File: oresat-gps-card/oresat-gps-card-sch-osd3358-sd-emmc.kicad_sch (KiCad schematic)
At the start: 65 parts, among them J4 DM3BT-DSF-PEJS, U1 OSD3358-512M-BSM, U8 TCAN330, U9 EMMC+RESET+5.1-COMPATIBLE-BA

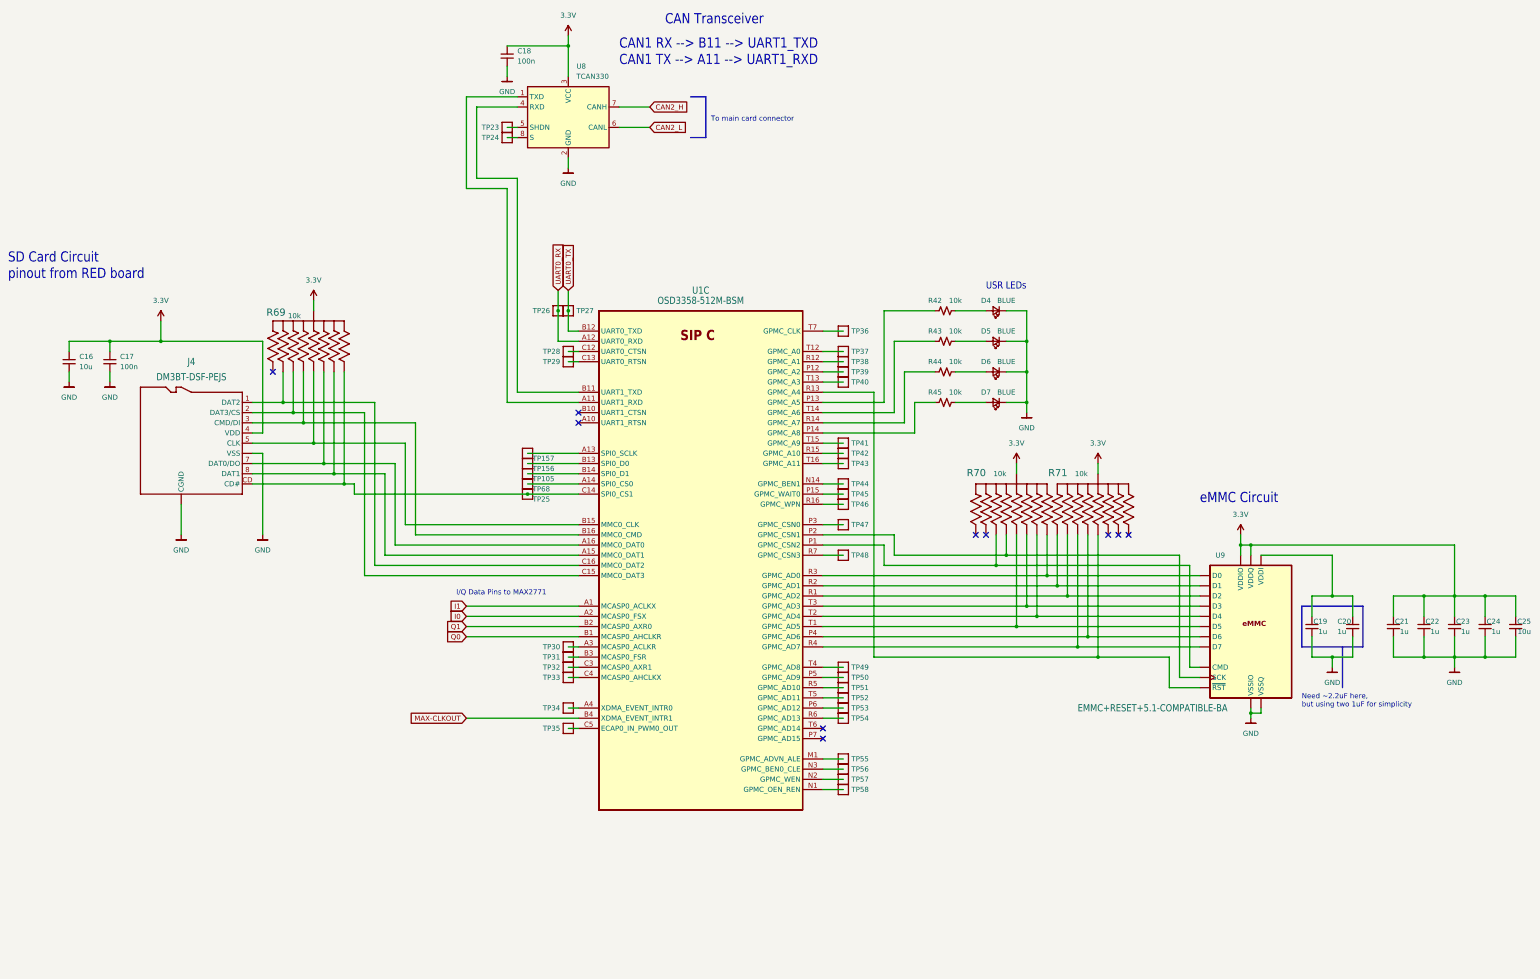
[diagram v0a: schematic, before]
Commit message: Cleaned up ERC and DRC errors on GPS card
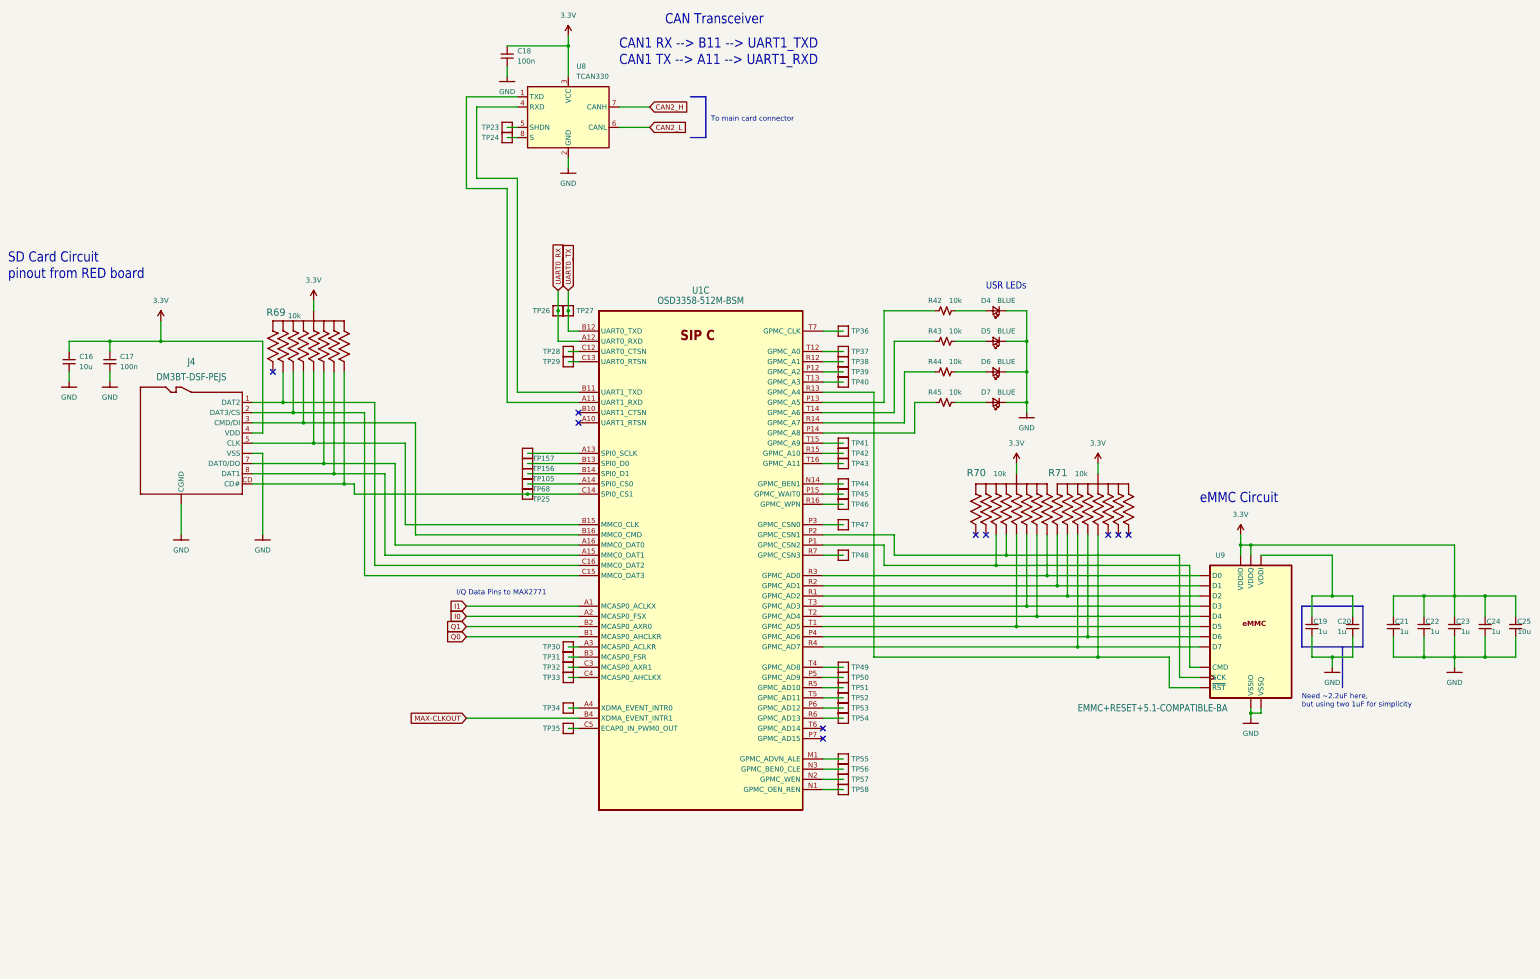
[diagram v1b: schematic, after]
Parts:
- J4: footprint oresat-footprints:J-Hirose-DM3BT-DSF-PEJS -> oresat-connectors:J-Hirose-DM3BT-DSF-PEJS
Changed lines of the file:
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@@
       (effects (font (size 1.778 1.5113)))
     )
-    (property "Footprint" "oresat-footprints:J-Hirose-DM3BT-DSF-PEJS" (at 66.04 129.54 0)
+    (property "Footprint" "oresat-connectors:J-Hirose-DM3BT-DSF-PEJS" (at 66.04 129.54 0)
       (effects (font (size 1.27 1.27)) hide)
     )

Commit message: Updated KiCAD 8, updated schematic sheet info, polished some schematic things, and made DNP parts DNP.
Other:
- title: (none) -> OreSat GPS Card

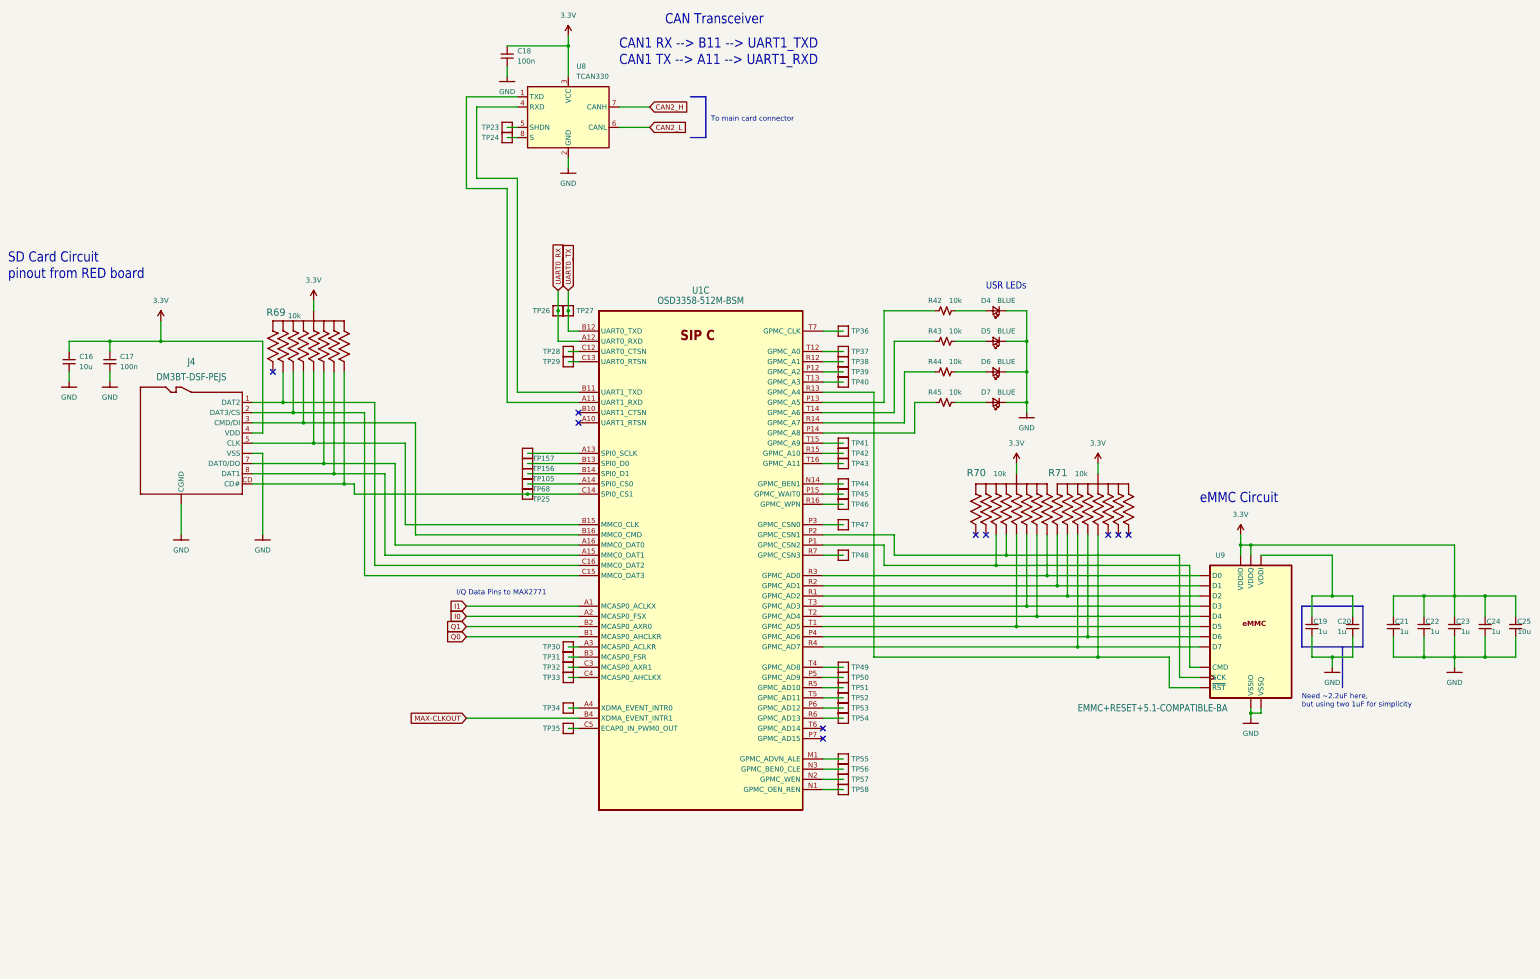
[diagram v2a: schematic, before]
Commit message: updated symbols and started new 2771 symbol
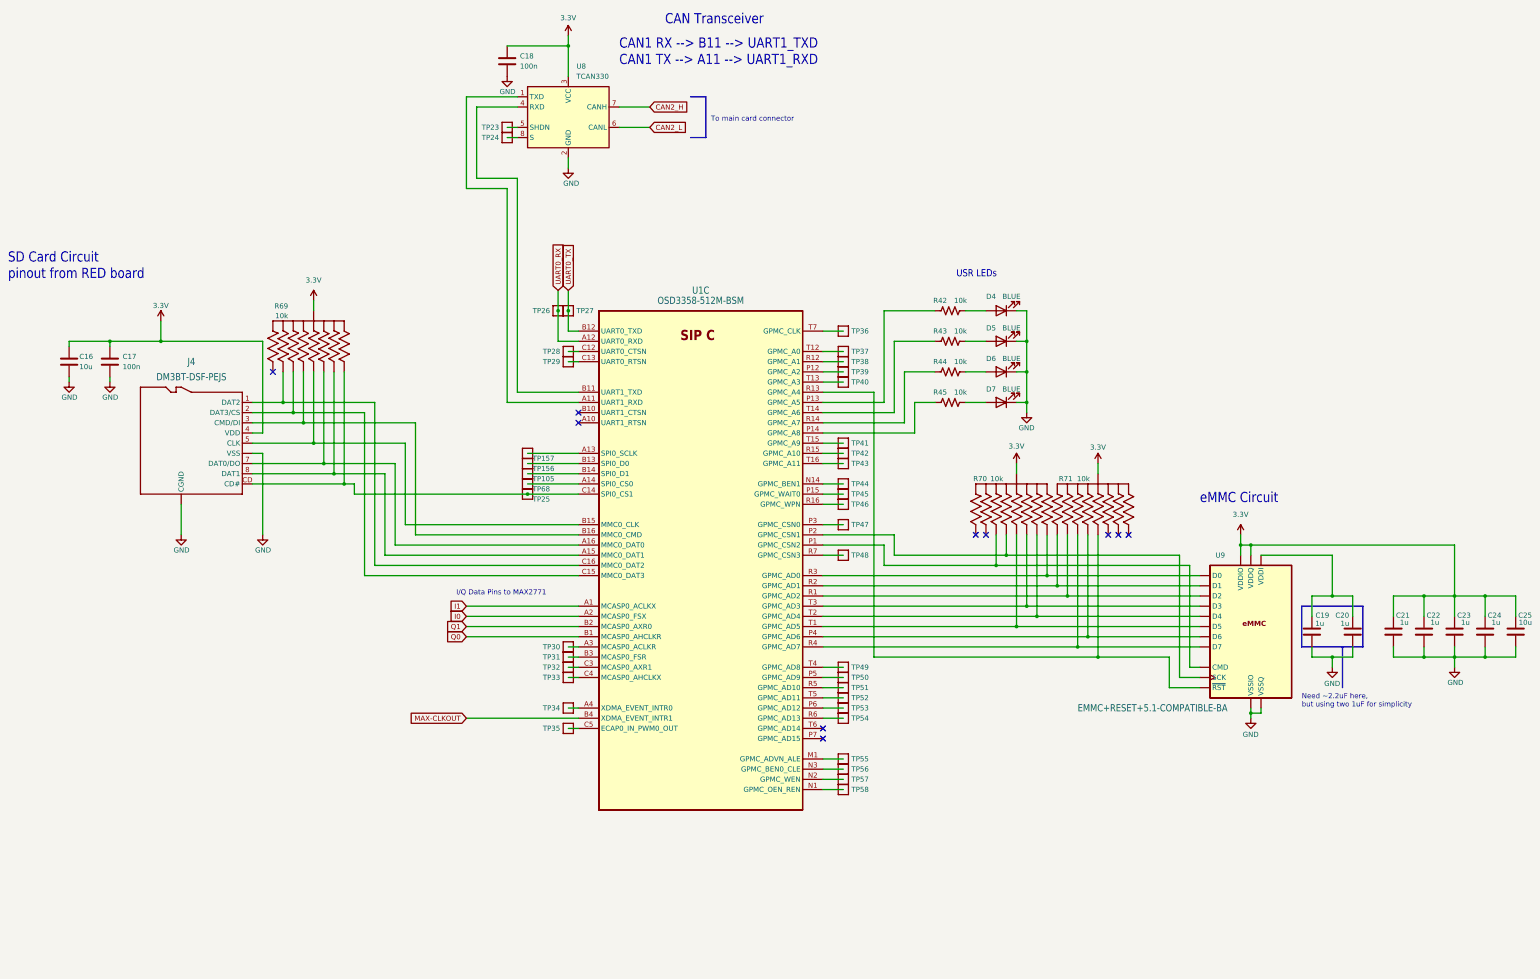
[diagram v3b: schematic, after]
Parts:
- C16, C17, C18, C19, C20, C21, C22, C23, C24, C25: symbol Device:C_Small -> Device:C
- D4, D5, D6, D7: symbol Device:LED_Small -> Device:LED
- R42, R43, R44, R45: symbol Device:R_Small_US -> Device:R_US
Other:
- moved on the sheet: C18, C19, C20, C21, C22, C23, C24, C25, D4, D5, D6, D7

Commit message: Routine Push
Various small changes made
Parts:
- removed TP105, TP156, TP157, TP23, TP24, TP25, TP28, TP29, TP30, TP31, TP32, TP33, TP34, TP35, TP36, TP37, TP38, TP39, TP40, TP41, TP42, TP43, TP44, TP45, TP46, TP47, TP48, TP49, TP50, TP51, TP52, TP53, TP54, TP55, TP56, TP57, TP58, TP68: 0.03x0.04, oresat-misc:TestPoint_Pad_D1.0mm, symbol oresat-misc:Test-Point-1mm-round
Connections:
- no-connect marks 10 -> 45

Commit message: Routine Push
First attempt to clean up schematic
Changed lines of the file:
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@@
 		)
 	)
-	(global_label "I1"
+	(hierarchical_label "Q0"
 		(shape input)
-		(at 134.62 170.18 180)
-		(fields_autoplaced yes)
+		(at 134.62 177.8 180)
 		(effects
 			(font
@@
 			(justify right)
 		)
-		(property "Intersheetrefs" "${INTERSHEET_REFS}"
-			(at 130.3926 170.1006 0)
-			(show_name no)
-			(do_not_autoplace no)
-			(effects
-				(font
-					(size 1.27 1.27)
-				)
-				(justify right)
-			)
-		)
 	)
-	(global_label "Q0"
+	(hierarchical_label "Q1"
 		(shape input)
-		(at 134.62 177.8 180)
-		(fields_autoplaced yes)
+		(at 134.62 175.26 180)
 		(effects
 			(font
@@
 			(justify right)
 		)
-		(property "Intersheetrefs" "${INTERSHEET_REFS}"
-			(at 129.6669 177.7206 0)
-			(show_name no)
-			(do_not_autoplace no)
-			(effects
-				(font
-					(size 1.27 1.27)
-				)
-				(justify right)
+	)
+	(hierarchical_label "UART0_TX"
+		(shape input)
+		(at 160.02 91.44 90)
+		(effects
+			(font
+				(size 1.27 1.27)
 			)
+			(justify left)
 		)
 	)
-	(global_label "MAX-CLKOUT"
+	(hierarchical_label "CAN2_L"
+		(shape input)
+		(at 180.34 50.8 0)
+		(effects
+			(font
+				(size 1.27 1.27)
+			)
+			(justify left)
+		)
+	)
+	(hierarchical_label "MAX-CLKOUT"
 		(shape input)
 		(at 134.62 198.12 180)
-		(fields_autoplaced yes)
 		(effects
 			(font
@@
 			(justify right)
 		)
-		(property "Intersheetrefs" "${INTERSHEET_REFS}"
-			(at 119.6883 198.0406 0)
-			(show_name no)
-			(do_not_autoplace no)
-			(effects
-				(font
-					(size 1.27 1.27)
-				)
-				(justify right)
+	)
+	(hierarchical_label "UART0_RX"
+		(shape output)
+		(at 157.48 91.44 90)
+		(effects
+			(font
+				(size 1.27 1.27)
 			)
+			(justify left)
 		)
 	)
-	(global_label "Q1"
+	(hierarchical_label "CAN2_H"
 		(shape input)
-		(at 134.62 175.26 180)
-		(fields_autoplaced yes)
+		(at 180.34 45.72 0)
+		(effects
+			(font
+				(size 1.27 1.27)
+			)
+			(justify left)
+		)
+	)
+	(hierarchical_label "I1"
+		(shape input)
+		(at 134.62 170.18 180)
 		(effects
 			(font
@@
 			(justify right)
 		)
-		(property "Intersheetrefs" "${INTERSHEET_REFS}"
-			(at 129.6669 175.1806 0)
-			(show_name no)
-			(do_not_autoplace no)
-			(effects
-				(font
-					(size 1.27 1.27)
-				)
-				(justify right)
-			)
-		)
 	)
-	(global_label "UART0_RX"
-		(shape input)
-		(at 157.48 91.44 90)
-		(fields_autoplaced yes)
-		(effects
-			(font
-				(size 1.27 1.27)
-			)
-			(justify left)
-		)
-		(property "Intersheetrefs" "${INTERSHEET_REFS}"
-			(at 157.4006 79.7136 90)
-			(show_name no)
-			(do_not_autoplace no)
-			(effects
-				(font
-					(size 1.27 1.27)
-				)
-				(justify left)
-			)
-		)
-	)
-	(global_label "CAN2_L"
-		(shape input)
-		(at 180.34 50.8 0)
-		(fields_autoplaced yes)
-		(effects
-			(font
-				(size 1.27 1.27)
-			)
-			(justify left)
-		)
-		(property "Intersheetrefs" "${INTERSHEET_REFS}"
-			(at 189.6474 50.7206 0)
-			(show_name no)
-			(do_not_autoplace no)
-			(effects
-				(font
-					(size 1.27 1.27)
-				)
-				(justify left)
-			)
-		)
-	)
-	(global_label "I0"
+	(hierarchical_label "I0"
 		(shape input)
 		(at 134.62 172.72 180)
-		(fields_autoplaced yes)
 		(effects
 			(font
@@
 			(justify right)
 		)
-		(property "Intersheetrefs" "${INTERSHEET_REFS}"
-			(at 130.3926 172.6406 0)
-			(show_name no)
-			(do_not_autoplace no)
-			(effects
-				(font
-					(size 1.27 1.27)
-				)
-				(justify right)
-			)
-		)
 	)
-	(global_label "CAN2_H"
-		(shape input)
-		(at 180.34 45.72 0)
-		(fields_autoplaced yes)
-		(effects
-			(font
-				(size 1.27 1.27)
-			)
-			(justify left)
-		)
-		(property "Intersheetrefs" "${INTERSHEET_REFS}"
-			(at 189.9498 45.6406 0)
-			(show_name no)
-			(do_not_autoplace no)
-			(effects
-				(font
-					(size 1.27 1.27)
-				)
-				(justify left)
-			)
-		)
-	)
-	(global_label "UART0_TX"
-		(shape input)
-		(at 160.02 91.44 90)
-		(fields_autoplaced yes)
-		(effects
-			(font
-				(size 1.27 1.27)
-			)
-			(justify left)
-		)
-		(property "Intersheetrefs" "${INTERSHEET_REFS}"
-			(at 159.9406 80.0159 90)
-			(show_name no)
-			(do_not_autoplace no)
-			(effects
-				(font
-					(size 1.27 1.27)
-				)
-				(justify left)
-			)
-		)
-	)

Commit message: Routine Push
Schematic finished. Components laid out, chasing ERCs.
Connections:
- no-connect marks 45 -> 47
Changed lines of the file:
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@@
 	)
 	(junction
-		(at 350.52 182.88)
-		(diameter 0)
-		(color 0 0 0 0)
-	)
-	(junction
 		(at 160.02 96.52)
 		(diameter 0)
@@
 	)
 	(junction
-		(at 284.48 167.64)
+		(at 350.52 167.64)
 		(diameter 0)
 		(color 0 0 0 0)
 	)
 	(junction
-		(at 274.32 170.18)
+		(at 284.48 167.64)
 		(diameter 0)
 		(color 0 0 0 0)
 	)
 	(junction
-		(at 350.52 167.64)
+		(at 274.32 170.18)
 		(diameter 0)
 		(color 0 0 0 0)
@@
 	)
 	(junction
+		(at 350.52 182.88)
+		(diameter 0)
+		(color 0 0 0 0)
+	)
+	(junction
 		(at 279.4 162.56)
 		(diameter 0)
@@
 	)
 	(no_connect
+		(at 147.32 53.34)
+	)
+	(no_connect
 		(at 223.52 101.6)
 	)
@@
 	)
 	(no_connect
+		(at 147.32 50.8)
+	)
+	(no_connect
 		(at 223.52 210.82)
 	)
@@
 	(wire
 		(pts
+			(xy 350.52 182.88) (xy 350.52 185.42)
+		)
+		(stroke
+			(width 0)
+			(type default)
+		)
+	)
+	(wire
+		(pts
 			(xy 281.94 152.4) (xy 281.94 165.1)
 		)
@@
 	(wire
 		(pts
+			(xy 350.52 182.88) (xy 355.6 182.88)
+		)
+		(stroke
+			(width 0)
+			(type default)
+		)
+	)
+	(wire
+		(pts
 			(xy 160.02 30.48) (xy 160.02 38.1)
 		)
@@
 		)
 	)
+	(wire
+		(pts
+			(xy 345.44 167.64) (xy 350.52 167.64)
+		)
+		(stroke
+			(width 0)
+			(type default)
+		)
+	)
 	(polyline
 		(pts
@@
 	(wire
 		(pts
-			(xy 350.52 182.88) (xy 350.52 185.42)
-		)
-		(stroke
-			(width 0)
-			(type default)
-		)
-	)
-	(wire
-		(pts
 			(xy 106.68 142.24) (xy 162.56 142.24)
 		)
@@
 	(wire
 		(pts
+			(xy 350.52 167.64) (xy 355.6 167.64)
+		)
+		(stroke
+			(width 0)
+			(type default)
+		)
+	)
+	(wire
+		(pts
 			(xy 147.32 63.5) (xy 137.16 63.5)
 		)
@@
 	(wire
 		(pts
-			(xy 355.6 182.88) (xy 350.52 182.88)
+			(xy 345.44 182.88) (xy 350.52 182.88)
 		)
 		(stroke
@@
 	(wire
 		(pts
-			(xy 345.44 182.88) (xy 350.52 182.88)
-		)
-		(stroke
-			(width 0)
-			(type default)
-		)
-	)
-	(wire
-		(pts
 			(xy 45.72 104.14) (xy 58.42 104.14)
 		)
@@
 	(wire
 		(pts
-			(xy 350.52 167.64) (xy 350.52 157.48)
+			(xy 312.42 187.96) (xy 312.42 157.48)
 		)
 		(stroke
@@
 	(wire
 		(pts
-			(xy 312.42 187.96) (xy 312.42 157.48)
+			(xy 241.3 104.14) (xy 251.46 104.14)
 		)
 		(stroke
@@
 	(wire
 		(pts
-			(xy 241.3 104.14) (xy 251.46 104.14)
+			(xy 396.24 182.88) (xy 388.62 182.88)
 		)
 		(stroke
@@
 	(wire
 		(pts
-			(xy 396.24 182.88) (xy 388.62 182.88)
+			(xy 259.08 111.76) (xy 264.16 111.76)
 		)
 		(stroke
@@
 		)
 	)
-	(wire
+	(polyline
 		(pts
-			(xy 259.08 111.76) (xy 264.16 111.76)
+			(xy 194.31 43.18) (xy 194.31 53.34)
 		)
 		(stroke
@@
 		)
 	)
-	(polyline
+	(wire
 		(pts
-			(xy 194.31 43.18) (xy 194.31 53.34)
+			(xy 350.52 157.48) (xy 350.52 167.64)
 		)
 		(stroke
@@
 	(wire
 		(pts
-			(xy 355.6 167.64) (xy 350.52 167.64)
-		)
-		(stroke
-			(width 0)
-			(type default)
-		)
-	)
-	(wire
-		(pts
-			(xy 345.44 167.64) (xy 350.52 167.64)
-		)
-		(stroke
-			(width 0)
-			(type default)
-		)
-	)
-	(wire
-		(pts
 			(xy 223.52 170.18) (xy 274.32 170.18)
 		)
@@
 			)
 		)
-		(property "Datasheet" ""
+		(property "Datasheet" "https://octavosystems.com/docs/osd335x-sm-datasheet/"
 			(at 193.04 157.48 0)
 			(hide yes)

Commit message: Routine Push
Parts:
- removed D4, D5, D6: BLUE, LED_SMD:LED_0603_1608Metric, symbol Device:LED
- removed R42, R43, R44: 10k, Resistor_SMD:R_0603_1608Metric, symbol Device:R_US
- C16, C25: footprint Capacitor_SMD:C_0805_2012Metric -> Capacitor_SMD:C_0603_1608Metric
- TP26, TP27: footprint oresat-misc:TestPoint_Pad_D1.0mm -> oresat-misc:TestPoint-0.75mm-th
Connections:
- no-connect marks 47 -> 50
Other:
- note added: "All resistors are 0603 1% AEC-Q200 unless marked. All capacitors are 0603 AEC-Q200 Vw >= 16V X5R or better unless marked."
- note removed: "USR LEDs"
